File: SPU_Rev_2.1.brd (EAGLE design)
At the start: 127.6 x 101.6 mm, 251 parts, among them Q1 12MHz

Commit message: finished routing
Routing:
- net STRUCT: track 0.04 -> 367.9 mm
- net GND: track 1186.2 -> 1440.6 mm, vias 102 -> 117
- net 28VGND: track 111.6 -> 302.0 mm, vias 5 -> 10
- net !DRDY!_PT2: track 4.29 -> 69.1 mm, vias 2 -> 5
- net LED_2: track 0.00 -> 61.0 mm, vias 0 -> 4
- net LED_3: track 0.00 -> 57.4 mm, vias 0 -> 3
- net LO_OPT: track 93.5 -> 107.9 mm, vias 4 -> 6
- net SOE_OPT: track 84.9 -> 97.0 mm, vias 4 -> 5
- net N$45: track 0.00 -> 4.55 mm, vias 0 -> 1
- net MS_SEL: track 9.32 -> 13.2 mm, vias 0 -> 1
- net N$11: track 8.65 -> 10.8 mm, vias 1 -> 2
- net LED_1: track 59.5 -> 61.6 mm
- net 3V3: track 845.6 -> 847.7 mm
- net PT22: track 39.9 -> 41.2 mm
- net !DRDY!_PT1: track 40.8 -> 42.1 mm
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
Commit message: Update SPU_Rev_2.1.brd
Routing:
- net 3V3: track 847.7 -> 847.1 mm
- net GND: track 1440.6 -> 1440.1 mm, vias 117 -> 168
- net 28VGND: vias 10 -> 25
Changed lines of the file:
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@@
 <contactref element="X_PT" pad="P$A6"/>
 <contactref element="X_PT" pad="P$A5"/>
-<wire x1="19.6469" y1="91.846840625" x2="19.615" y2="91.831" width="0.2032" layer="1"/>
-<wire x1="19.6469" y1="93.062609375" x2="19.615" y2="93.081" width="0.2032" layer="1"/>
 <wire x1="46.091" y1="74.365" x2="46.0845" y2="74.3585" width="0.2032" layer="1"/>
 <wire x1="46.3804" y1="74.3585" x2="46.0845" y2="74.3585" width="0.2032" layer="1"/>
-<wire x1="44.196" y1="87.6173" x2="44.079" y2="87.573" width="0.2032" layer="1"/>
 <wire x1="47.0662" y1="16.8402" x2="46.4185" y2="16.8402" width="0.2032" layer="1"/>
 <wire x1="46.4185" y1="16.8402" x2="46.456" y2="16.7608" width="0.2032" layer="1"/>
@@
 <wire x1="50.3047" y1="64.9859" x2="50.504346875" y2="65.166596875" width="0.2032" layer="1"/>
 <wire x1="34.9758" y1="75.1332" x2="33.0327" y2="75.1332" width="0.2032" layer="1"/>
-<wire x1="30.4419" y1="75.7809" x2="30.226" y2="75.565" width="0.2032" layer="1"/>
 <wire x1="34.9758" y1="75.1332" x2="35.1822" y2="75.083" width="0.2032" layer="1"/>
 <wire x1="30.4419" y1="75.7809" x2="30.519" y2="75.819" width="0.2032" layer="1"/>
@@
 <wire x1="58.42" y1="75.7936" x2="60.0964" y2="77.47" width="0.2032" layer="2"/>
 <wire x1="60.0964" y1="77.47" x2="63.373" y2="77.47" width="0.2032" layer="2"/>
+<via x="17.272" y="45.466" extent="1-16" drill="0.35"/>
+<via x="25.781" y="45.339" extent="1-16" drill="0.35"/>
+<via x="32.766" y="45.212" extent="1-16" drill="0.35"/>
+<via x="40.64" y="45.339" extent="1-16" drill="0.35"/>
+<via x="44.069" y="36.195" extent="1-16" drill="0.35"/>
+<via x="38.735" y="28.067" extent="1-16" drill="0.35"/>
+<via x="31.496" y="27.686" extent="1-16" drill="0.35"/>
+<via x="20.701" y="27.686" extent="1-16" drill="0.35"/>
+<via x="15.748" y="36.703" extent="1-16" drill="0.35"/>
+<via x="12.827" y="26.543" extent="1-16" drill="0.35"/>
+<via x="44.577" y="27.051" extent="1-16" drill="0.35"/>
+<via x="47.752" y="25.654" extent="1-16" drill="0.35"/>
+<via x="56.769" y="40.259" extent="1-16" drill="0.35"/>
+<via x="59.309" y="32.512" extent="1-16" drill="0.35"/>
+<via x="26.797" y="51.562" extent="1-16" drill="0.35"/>
+<via x="12.446" y="77.597" extent="1-16" drill="0.35"/>
+<via x="12.192" y="84.328" extent="1-16" drill="0.35"/>
+<via x="51.054" y="94.742" extent="1-16" drill="0.35"/>
+<via x="67.31" y="93.98" extent="1-16" drill="0.35"/>
+<via x="82.169" y="94.742" extent="1-16" drill="0.35"/>
+<via x="90.043" y="95.25" extent="1-16" drill="0.35"/>
+<via x="101.092" y="95.123" extent="1-16" drill="0.35"/>
+<via x="101.346" y="82.931" extent="1-16" drill="0.35"/>
+<via x="102.87" y="74.168" extent="1-16" drill="0.35"/>
+<via x="103.632" y="69.088" extent="1-16" drill="0.35"/>
+<via x="90.17" y="57.785" extent="1-16" drill="0.35"/>
+<via x="91.186" y="50.038" extent="1-16" drill="0.35"/>
+<via x="92.075" y="43.053" extent="1-16" drill="0.35"/>
+<via x="91.694" y="36.195" extent="1-16" drill="0.35"/>
+<via x="83.693" y="35.179" extent="1-16" drill="0.35"/>
+<via x="86.106" y="9.525" extent="1-16" drill="0.35"/>
+<via x="106.553" y="16.891" extent="1-16" drill="0.35"/>
+<via x="107.188" y="27.051" extent="1-16" drill="0.35"/>
+<via x="100.965" y="28.956" extent="1-16" drill="0.35"/>
+<via x="105.664" y="10.033" extent="1-16" drill="0.35"/>
+<via x="65.532" y="13.081" extent="1-16" drill="0.35"/>
+<via x="64.262" y="9.271" extent="1-16" drill="0.35"/>
+<via x="59.817" y="7.112" extent="1-16" drill="0.35"/>
+<via x="56.515" y="12.319" extent="1-16" drill="0.35"/>
+<via x="52.832" y="19.431" extent="1-16" drill="0.35"/>
+<via x="38.608" y="11.176" extent="1-16" drill="0.35"/>
+<via x="40.767" y="11.176" extent="1-16" drill="0.35"/>
+<via x="12.827" y="6.985" extent="1-16" drill="0.35"/>
+<via x="63.881" y="72.39" extent="1-16" drill="0.35"/>
+<via x="64.262" y="61.595" extent="1-16" drill="0.35"/>
+<via x="71.628" y="65.532" extent="1-16" drill="0.35"/>
+<via x="90.805" y="65.532" extent="1-16" drill="0.35"/>
+<via x="91.948" y="63.881" extent="1-16" drill="0.35"/>
+<via x="91.567" y="74.041" extent="1-16" drill="0.35"/>
+<via x="97.409" y="75.565" extent="1-16" drill="0.35"/>
+<via x="105.156" y="71.755" extent="1-16" drill="0.35"/>
 </signal>
 <signal name="28V">
@@
 <wire x1="50.108" y1="80.448" x2="50.165" y2="80.391" width="0.3048" layer="1"/>
 <wire x1="49.857" y1="80.391" x2="50.165" y2="80.391" width="0.3048" layer="1"/>
-<wire x1="50.165" y1="80.391" x2="50.746" y2="80.391" width="0.3048" layer="1"/>
 <wire x1="49.857" y1="80.391" x2="50.292" y2="80.826" width="0.3048" layer="1"/>
 <wire x1="30.607" y1="8.763" x2="44.069" y2="8.763" width="2.032" layer="16"/>
@@
 <wire x1="82.4738" y1="81.6102" x2="81.48" y2="81.588" width="0.2032" layer="16"/>
 <wire x1="23.114" y1="11.8745" x2="24.6126" y2="11.8745" width="0.2032" layer="16"/>
-<wire x1="22.0218" y1="11.8745" x2="22.02815" y2="11.88085" width="0.2032" layer="16"/>
 <wire x1="24.6126" y1="11.8745" x2="24.765" y2="11.865" width="0.2032" layer="16"/>
 <wire x1="31.3055" y1="82.6897" x2="31.3055" y2="84.8487" width="0.2032" layer="16"/>
@@
 <wire x1="87.92845" y1="46.71695" x2="88.011" y2="46.6344" width="0.2032" layer="16"/>
 <wire x1="20.828" y1="13.081" x2="20.828" y2="13.0683" width="0.254" layer="16"/>
+<wire x1="22.0218" y1="11.8745" x2="23.114" y2="11.8745" width="0.254" layer="16"/>
 <wire x1="20.828" y1="13.0683" x2="22.0218" y2="11.8745" width="0.254" layer="16"/>
-<wire x1="22.0218" y1="11.8745" x2="23.114" y2="11.8745" width="0.254" layer="16"/>
 </signal>
 <signal name="DAPI_TX">
@@
 <wire x1="102.87" y1="60.452" x2="102.108" y2="60.452" width="0.2032" layer="2"/>
 <wire x1="123.273" y1="66.929" x2="123.273" y2="68.199" width="0.2032" layer="1"/>
+<via x="94.996" y="42.418" extent="1-16" drill="0.35"/>
+<via x="113.284" y="46.609" extent="1-16" drill="0.35"/>
+<via x="110.236" y="41.656" extent="1-16" drill="0.35"/>
+<via x="120.523" y="48.26" extent="1-16" drill="0.35"/>
+<via x="120.65" y="41.529" extent="1-16" drill="0.35"/>
+<via x="112.141" y="35.306" extent="1-16" drill="0.35"/>
+<via x="120.142" y="30.48" extent="1-16" drill="0.35"/>
+<via x="113.792" y="18.796" extent="1-16" drill="0.35"/>
+<via x="116.84" y="15.748" extent="1-16" drill="0.35"/>
+<via x="121.285" y="12.573" extent="1-16" drill="0.35"/>
+<via x="120.523" y="9.017" extent="1-16" drill="0.35"/>
+<via x="106.553" y="78.232" extent="1-16" drill="0.35"/>
+<via x="109.093" y="75.057" extent="1-16" drill="0.35"/>
+<via x="115.189" y="74.676" extent="1-16" drill="0.35"/>
+<via x="103.886" y="94.488" extent="1-16" drill="0.35"/>
 </signal>
 <signal name="LED_4">

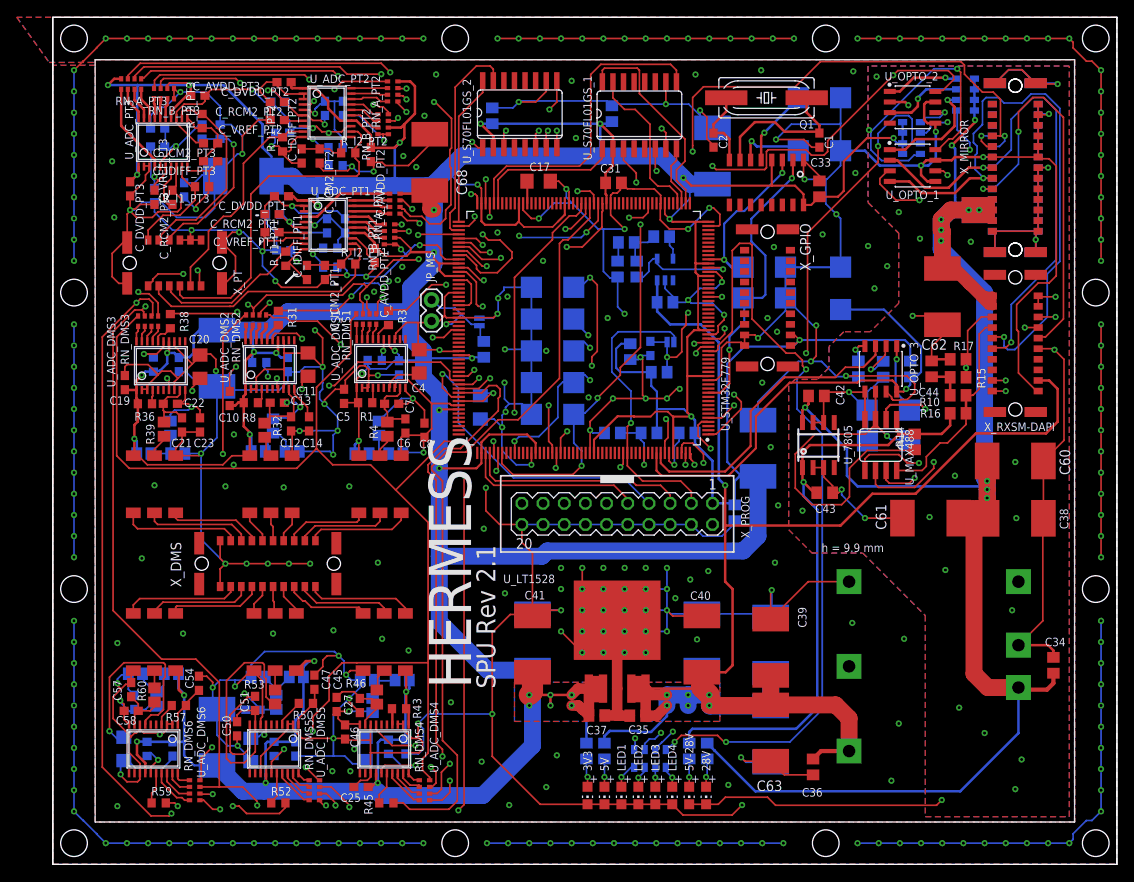
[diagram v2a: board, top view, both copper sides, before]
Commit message: finalized silkscreen
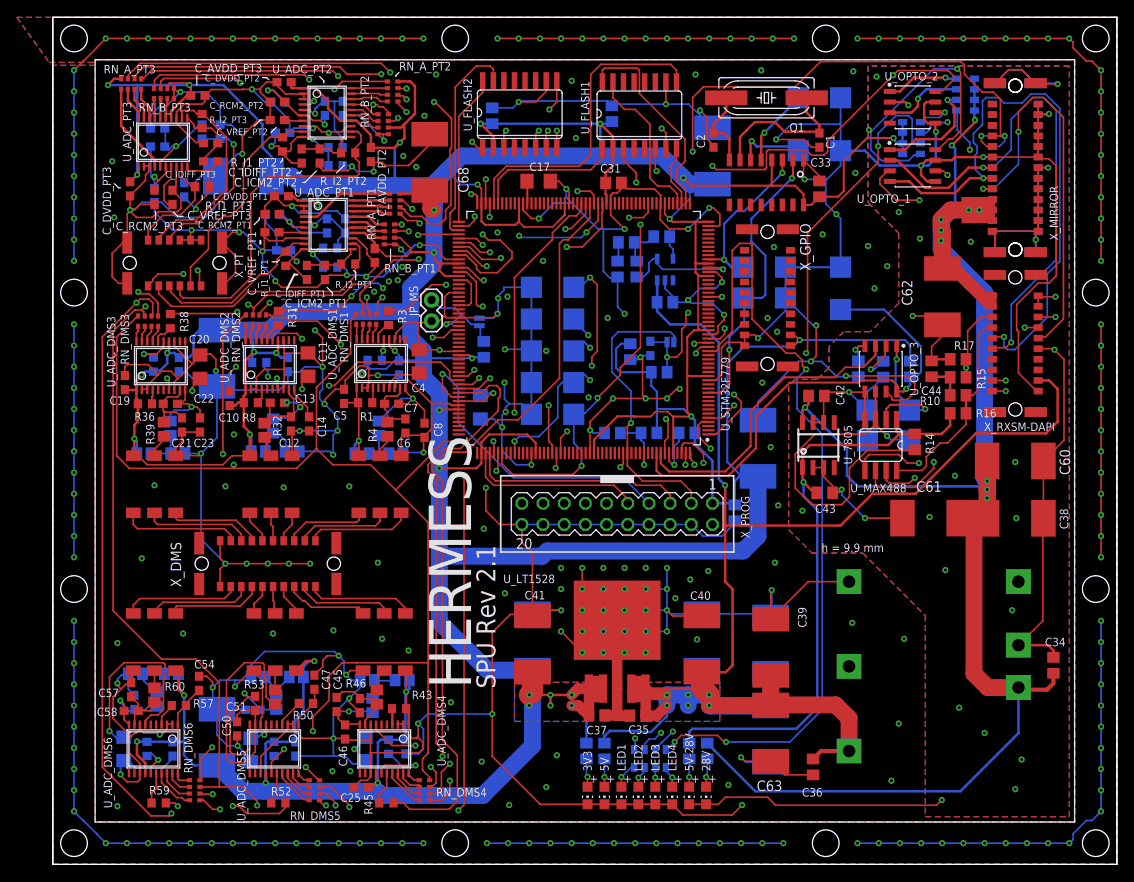
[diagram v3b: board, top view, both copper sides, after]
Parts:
- renumbered U_S70FL01GS_1 to U_FLASH1, U_S70FL01GS_2 to U_FLASH2

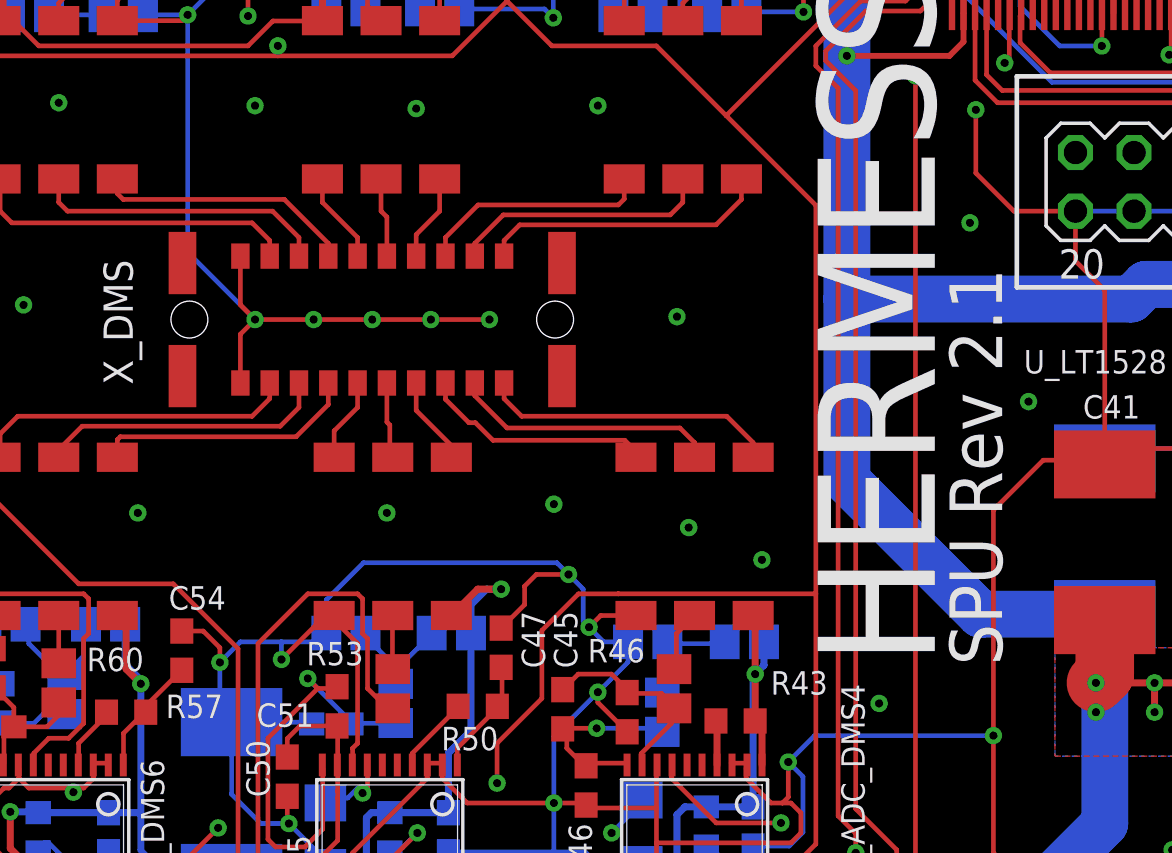
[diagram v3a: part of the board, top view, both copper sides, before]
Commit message: airwire fixed (2x)
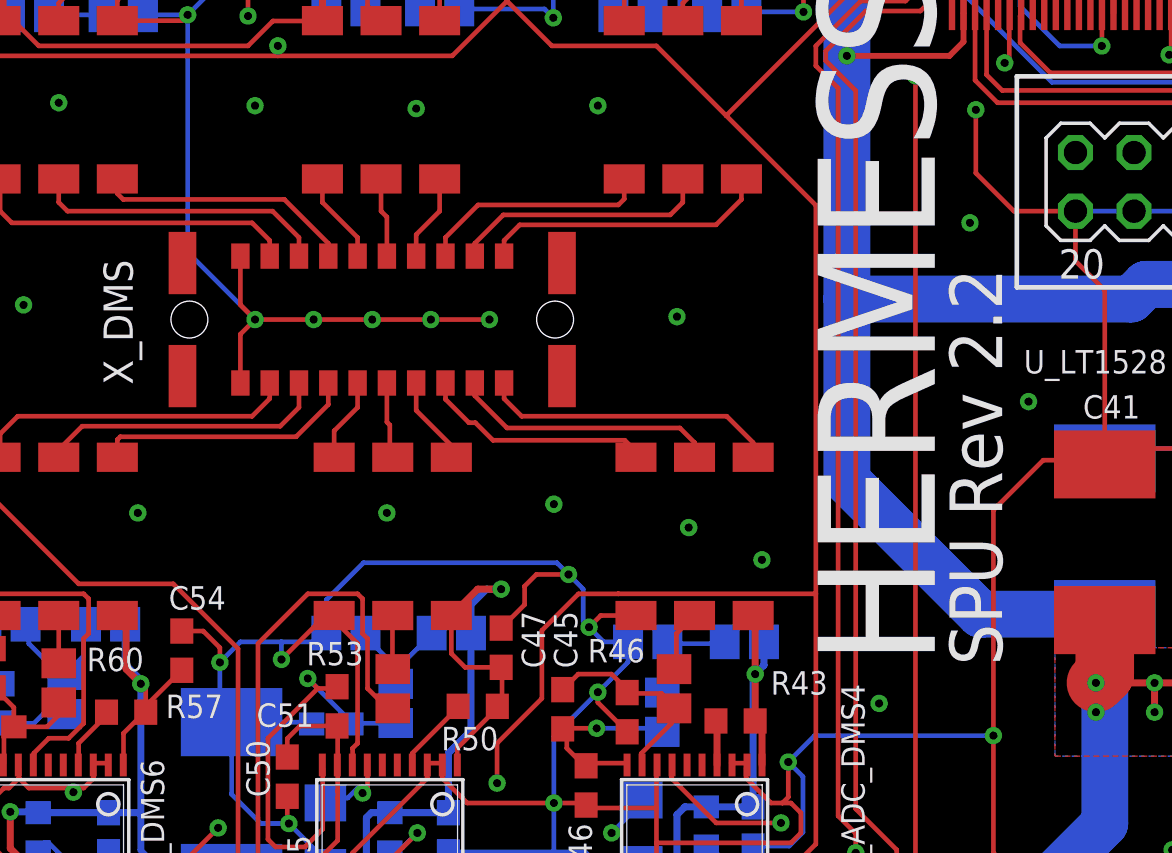
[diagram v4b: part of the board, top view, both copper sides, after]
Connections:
- removed net N$127: C47.1, R50.1, U_ADC_DMS5.1
- removed net N$141: C54.1, R57.1, U_ADC_DMS6.1
- net 3V3: now also C47.1, C54.1, R50.1, R57.1, U_ADC_DMS5.1, U_ADC_DMS6.1
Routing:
- net 3V3: track 847.1 -> 862.8 mm
- net N$141: track 5.25 -> 0.00 mm
- net N$127: track 5.08 -> 0.00 mm
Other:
- board text added: "SPU Rev 2.2"
- board text removed: "SPU Rev 2.1"
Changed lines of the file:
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@@
 <wire x1="5.08" y1="101.6" x2="132.715" y2="101.6" width="0.1524" layer="25"/>
 <text x="55.245" y="21.082" size="5.08" layer="25" font="vector" ratio="15" rot="R90">HERMESS</text>
-<text x="58.166" y="21.082" size="2.286" layer="25" font="vector" ratio="15" rot="R90">SPU Rev 2.1</text>
+<text x="58.166" y="21.082" size="2.286" layer="25" font="vector" ratio="15" rot="R90">SPU Rev 2.2</text>
 <wire x1="5.08" y1="101.6" x2="132.715" y2="101.6" width="0.1524" layer="26"/>
 <wire x1="132.715" y1="101.6" x2="132.715" y2="0" width="0.1524" layer="26"/>
@@
 <wire x1="22.0218" y1="11.8745" x2="23.114" y2="11.8745" width="0.254" layer="16"/>
 <wire x1="20.828" y1="13.0683" x2="22.0218" y2="11.8745" width="0.254" layer="16"/>
+<contactref element="U_ADC_DMS6" pad="1"/>
+<contactref element="C54" pad="1"/>
+<contactref element="R57" pad="1"/>
+<wire x1="20.0787" y1="18.1356" x2="20.0787" y2="16.8402" width="0.2032" layer="1"/>
+<wire x1="20.9423" y1="18.9992" x2="20.0787" y2="18.1356" width="0.2032" layer="1"/>
+<wire x1="20.0787" y1="16.8402" x2="20.07" y2="16.7608" width="0.2032" layer="1"/>
+<wire x1="20.9423" y1="18.9992" x2="21.043" y2="19.05" width="0.2032" layer="1"/>
+<wire x1="20.9423" y1="19.2151" x2="22.4536" y2="20.7264" width="0.2032" layer="1"/>
+<wire x1="22.4536" y1="20.7264" x2="22.606" y2="20.867" width="0.2032" layer="1"/>
+<wire x1="20.9423" y1="19.2151" x2="21.043" y2="19.05" width="0.2032" layer="1"/>
+<contactref element="U_ADC_DMS5" pad="1"/>
+<contactref element="C47" pad="1"/>
+<contactref element="R50" pad="1"/>
+<wire x1="34.544" y1="17.4879" x2="34.544" y2="16.8402" width="0.2032" layer="1"/>
+<wire x1="36.2712" y1="19.2151" x2="34.544" y2="17.4879" width="0.2032" layer="1"/>
+<wire x1="34.544" y1="16.8402" x2="34.548" y2="16.7608" width="0.2032" layer="1"/>
+<wire x1="36.2712" y1="19.2151" x2="36.283" y2="19.304" width="0.2032" layer="1"/>
+<wire x1="36.4871" y1="19.431" x2="36.4871" y2="20.9423" width="0.2032" layer="1"/>
+<wire x1="36.4871" y1="20.9423" x2="36.449" y2="20.994" width="0.2032" layer="1"/>
+<wire x1="36.4871" y1="19.431" x2="36.283" y2="19.304" width="0.2032" layer="1"/>
+<wire x1="36.449" y1="20.994" x2="34.886" y2="20.994" width="0.2032" layer="1"/>
+<wire x1="34.29" y1="21.59" x2="34.29" y2="23.239" width="0.2032" layer="1"/>
+<wire x1="34.886" y1="20.994" x2="34.29" y2="21.59" width="0.2032" layer="1"/>
+<wire x1="21.043" y1="19.05" x2="21.043" y2="20.068" width="0.2032" layer="1"/>
+<wire x1="21.043" y1="20.068" x2="20.828" y2="20.283" width="0.2032" layer="1"/>
 </signal>
 <signal name="DAPI_TX">
@@
 <wire x1="44.235" y1="8.3829" x2="44.235" y2="7.366" width="0.2032" layer="1"/>
 </signal>
-<signal name="N$127">
-<contactref element="U_ADC_DMS5" pad="1"/>
-<contactref element="C47" pad="1"/>
-<contactref element="R50" pad="1"/>
-<wire x1="34.544" y1="17.4879" x2="34.544" y2="16.8402" width="0.2032" layer="1"/>
-<wire x1="36.2712" y1="19.2151" x2="34.544" y2="17.4879" width="0.2032" layer="1"/>
-<wire x1="34.544" y1="16.8402" x2="34.548" y2="16.7608" width="0.2032" layer="1"/>
-<wire x1="36.2712" y1="19.2151" x2="36.283" y2="19.304" width="0.2032" layer="1"/>
-<wire x1="36.4871" y1="19.431" x2="36.4871" y2="20.9423" width="0.2032" layer="1"/>
-<wire x1="36.4871" y1="20.9423" x2="36.449" y2="20.994" width="0.2032" layer="1"/>
-<wire x1="36.4871" y1="19.431" x2="36.283" y2="19.304" width="0.2032" layer="1"/>
-</signal>
 <signal name="N$114">
 <contactref element="U_ADC_DMS5" pad="9"/>
@@
 <wire x1="33.2486" y1="22.4536" x2="33.44" y2="22.479" width="0.2032" layer="16"/>
 </signal>
-<signal name="N$141">
-<contactref element="U_ADC_DMS6" pad="1"/>
-<contactref element="C54" pad="1"/>
-<contactref element="R57" pad="1"/>
-<wire x1="20.0787" y1="18.1356" x2="20.0787" y2="16.8402" width="0.2032" layer="1"/>
-<wire x1="20.9423" y1="18.9992" x2="20.0787" y2="18.1356" width="0.2032" layer="1"/>
-<wire x1="20.0787" y1="16.8402" x2="20.07" y2="16.7608" width="0.2032" layer="1"/>
-<wire x1="20.9423" y1="18.9992" x2="21.043" y2="19.05" width="0.2032" layer="1"/>
-<wire x1="20.9423" y1="19.2151" x2="22.4536" y2="20.7264" width="0.2032" layer="1"/>
-<wire x1="22.4536" y1="20.7264" x2="22.606" y2="20.867" width="0.2032" layer="1"/>
-<wire x1="20.9423" y1="19.2151" x2="21.043" y2="19.05" width="0.2032" layer="1"/>
-</signal>
 <signal name="N$128">
